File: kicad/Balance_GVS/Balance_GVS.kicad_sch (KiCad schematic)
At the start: 0 parts

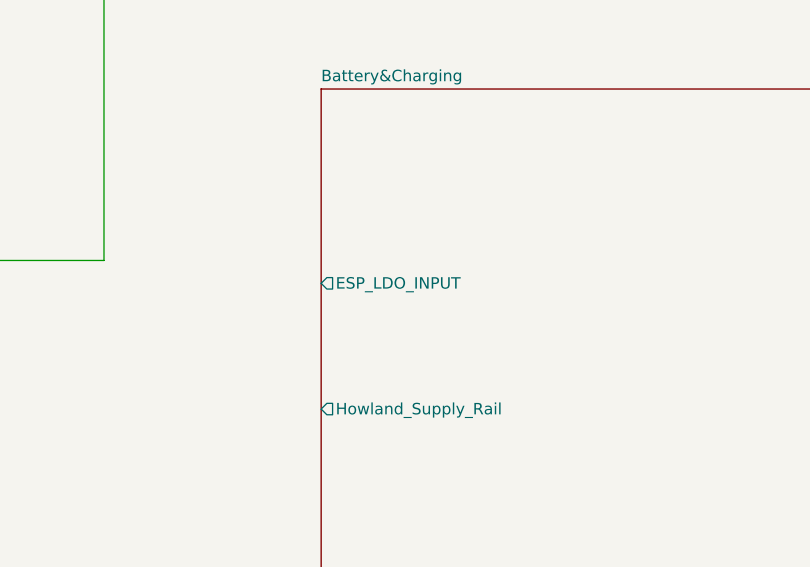
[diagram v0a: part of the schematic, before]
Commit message: Add 3.3V Voltage Regulator and ESP32 Battery ADC
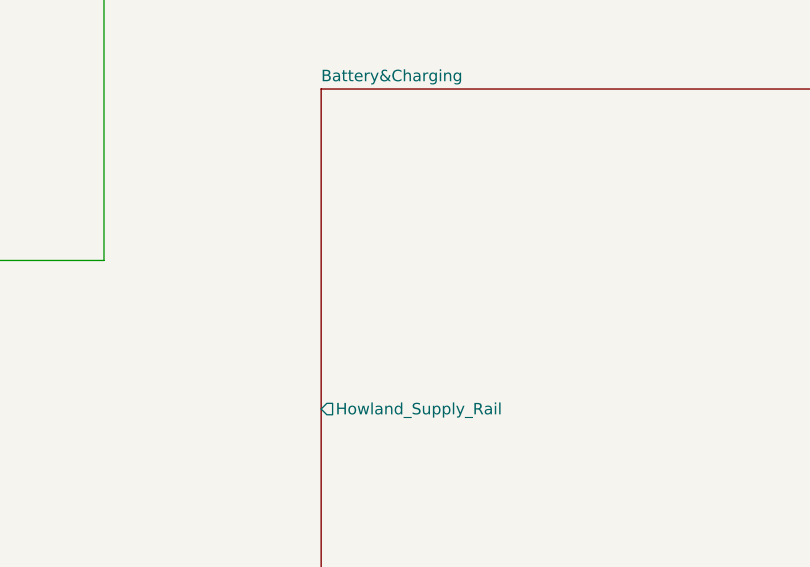
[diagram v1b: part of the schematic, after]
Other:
- sheet Battery&Charging ports: added none; removed ESP_LDO_INPUT
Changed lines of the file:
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@@
-			)
-		)
-		(pin "ESP_LDO_INPUT" output
-			(at 175.26 121.92 180)
-			(effects
-				(font
-					(size 1.27 1.27)
-				)
-				(justify left)
 			)
 		)

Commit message: Started adding howland connections
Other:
- sheet Battery&Charging ports: added none; removed Howland_Supply_Rail
- sheet HowlandPump ports: added none; removed Pump_Output
- sheet Safety ports: added none; removed Electrode+, Safety_Input
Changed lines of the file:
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@@
 	(generator_version "10.0")
 	(paper "A4")
-	(wire
-		(pts
-			(xy 135.89 119.38) (xy 151.13 119.38)
-		)
-		(stroke
-			(width 0)
-			(type default)
-		)
-	)
-	(wire
-		(pts
-			(xy 151.13 119.38) (xy 151.13 44.45)
-		)
-		(stroke
-			(width 0)
-			(type default)
-		)
-	)
-	(wire
-		(pts
-			(xy 151.13 44.45) (xy 173.99 44.45)
-		)
-		(stroke
-			(width 0)
-			(type default)
-		)
-	)
 	(sheet
 		(at 173.99 22.86)
@@
 				)
 				(justify left top)
-			)
-		)
-		(pin "Pump_Output" output
-			(at 173.99 44.45 180)
-			(effects
-				(font
-					(size 1.27 1.27)
-				)
-				(justify left)
 			)
 		)
@@
 			)
 		)
-		(pin "Howland_Supply_Rail" output
-			(at 175.26 135.89 180)
-			(effects
-				(font
-					(size 1.27 1.27)
-				)
-				(justify left)
-			)
-		)
 		(instances
 			(project "Balance_GVS"
@@
 			)
 		)
-		(pin "Safety_Input" input
-			(at 135.89 119.38 0)
-			(effects
-				(font
-					(size 1.27 1.27)
-				)
-				(justify right)
-			)
-		)
-		(pin "Electrode+" output
-			(at 135.89 137.16 0)
-			(effects
-				(font
-					(size 1.27 1.27)
-				)
-				(justify right)
-			)
-		)

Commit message: partial non-battery PCB now moved
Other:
- removed sheet Battery&Charging
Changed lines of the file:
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@@
-	)
-	(sheet
-		(at 175.26 100.33)
-		(size 76.2 54.61)
-		(exclude_from_sim no)
-		(in_bom yes)
-		(on_board yes)
-		(dnp no)
-		(fields_autoplaced yes)
-		(stroke
-			(width 0.1524)
-			(type solid)
-		)
-		(fill
-			(color 0 0 0 0)
-		)
-		(property "Sheetname" "Battery&Charging"
-			(at 175.26 99.6184 0)
-			(show_name no)
-			(do_not_autoplace no)
-			(effects
-				(font
-					(size 1.27 1.27)
-				)
-				(justify left bottom)
-			)
-		)
-		(property "Sheetfile" "Battery&Charging.kicad_sch"
-			(at 175.26 155.5246 0)
-			(show_name no)
-			(do_not_autoplace no)
-			(effects
-				(font
-					(size 1.27 1.27)
-				)
-				(justify left top)
-			)
-		)
-		(instances
-			(project "Balance_GVS"
-				(path "/fe65ed2a-e0ad-4542-81bb-0c202b789e4d"
-					(page "3")
-				)
-			)
-		)
 	)
 	(sheet

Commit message: I kinda popped off ngl. Main pcb almost done
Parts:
- added H1, H2: MountingHole, MountingHole:MountingHole_3.5mm, symbol Mechanical:MountingHole
- added J14: B3B-XH-A, B3B_XH_A:JST_B3B-XH-A, symbol B3B_XH_A:B3B-XH-A
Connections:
- new net +24V: J14.3
- new net Battery_Voltage: J14.1
- new net GND: J14.2
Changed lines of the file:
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@@
 	(generator_version "10.0")
 	(paper "A4")
-	(sheet
-		(at 173.99 22.86)
-		(size 77.47 57.15)
-		(exclude_from_sim no)
-		(in_bom yes)
-		(on_board yes)
-		(dnp no)
-		(fields_autoplaced yes)
-		(stroke
-			(width 0.1524)
-			(type solid)
-		)
-		(fill
-			(color 0 0 0 0)
-		)
-		(property "Sheetname" "HowlandPump"
-			(at 173.99 22.1484 0)
-			(show_name no)
-			(do_not_autoplace no)
-			(effects
-				(font
-					(size 1.27 1.27)
-				)
-				(justify left bottom)
-			)
-		)
-		(property "Sheetfile" "HowlandPump.kicad_sch"
-			(at 173.99 80.5946 0)
-			(show_name no)
-			(do_not_autoplace no)
-			(effects
-				(font
-					(size 1.27 1.27)
-				)
-				(justify left top)
-			)
-		)
-		(instances
-			(project "Balance_GVS"
-				(path "/fe65ed2a-e0ad-4542-81bb-0c202b789e4d"
-					(page "4")
-				)
-			)
-		)
-	)
-	(sheet
-		(at 49.53 20.32)
-		(size 60.96 52.07)
-		(exclude_from_sim no)
-		(in_bom yes)
-		(on_board yes)
-		(dnp no)
-		(fields_autoplaced yes)
-		(stroke
-			(width 0.1524)
-			(type solid)
-		)
-		(fill
-			(color 0 0 0 0)
-		)
-		(property "Sheetname" "Processor"
-			(at 49.53 19.6084 0)
-			(show_name no)
-			(do_not_autoplace no)
-			(effects
-				(font
-					(size 1.27 1.27)
-				)
-				(justify left bottom)
-			)
-		)
-		(property "Sheetfile" "Processor.kicad_sch"
-			(at 49.53 72.9746 0)
-			(show_name no)
-			(do_not_autoplace no)
-			(effects
-				(font
-					(size 1.27 1.27)
-				)
-				(justify left top)
-			)
-		)
-		(instances
-			(project "Balance_GVS"
-				(path "/fe65ed2a-e0ad-4542-81bb-0c202b789e4d"
-					(page "2")
-				)
-			)
-		)
-	)
-	(sheet
-		(at 57.15 101.6)
-		(size 78.74 52.07)
-		(exclude_from_sim no)
-		(in_bom yes)
-		(on_board yes)
-		(dnp no)
-		(fields_autoplaced yes)
-		(stroke
-			(width 0.1524)
-			(type solid)
-		)
-		(fill
-			(color 0 0 0 0)
-		)
-		(property "Sheetname" "Safety"
-			(at 57.15 100.8884 0)
-			(show_name no)
-			(do_not_autoplace no)
-			(effects
-				(font
-					(size 1.27 1.27)
-				)
-				(justify left bottom)
-			)
-		)
-		(property "Sheetfile" "Safety.kicad_sch"
-			(at 57.15 154.2546 0)
-			(show_name no)
-			(do_not_autoplace no)
-			(effects
-				(font
-					(size 1.27 1.27)
-				)
-				(justify left top)
-			)
-		)
-		(instances
-			(project "Balance_GVS"
-				(path "/fe65ed2a-e0ad-4542-81bb-0c202b789e4d"
-					(page "5")
-				)
-			)
-		)
-	)
-	(sheet_instances
-		(path "/"
-			(page "1")
-		)
-	)
-	(embedded_fonts no)
-)
